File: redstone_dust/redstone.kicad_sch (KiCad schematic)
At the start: 42 parts, among them J1 Conn_01x04_MountingPin, J2 Conn_01x04_MountingPin, J3 Conn_01x04_MountingPin, J4 Conn_01x04_MountingPin, J5 Conn_01x04_MountingPin, J6 Conn_01x04_MountingPin, J7 Conn_01x04_MountingPin, J8 Conn_01x04_MountingPin, Q1 BC108, Q2 BC108, Q3 BC108, Q4 BC108, SW1 SW_Push_Open, U1 RP2040, U2 RBT05W24S05, U3 TPS62162DSG, U4 W25Q16JVSS, U5 W25Q16JVSS

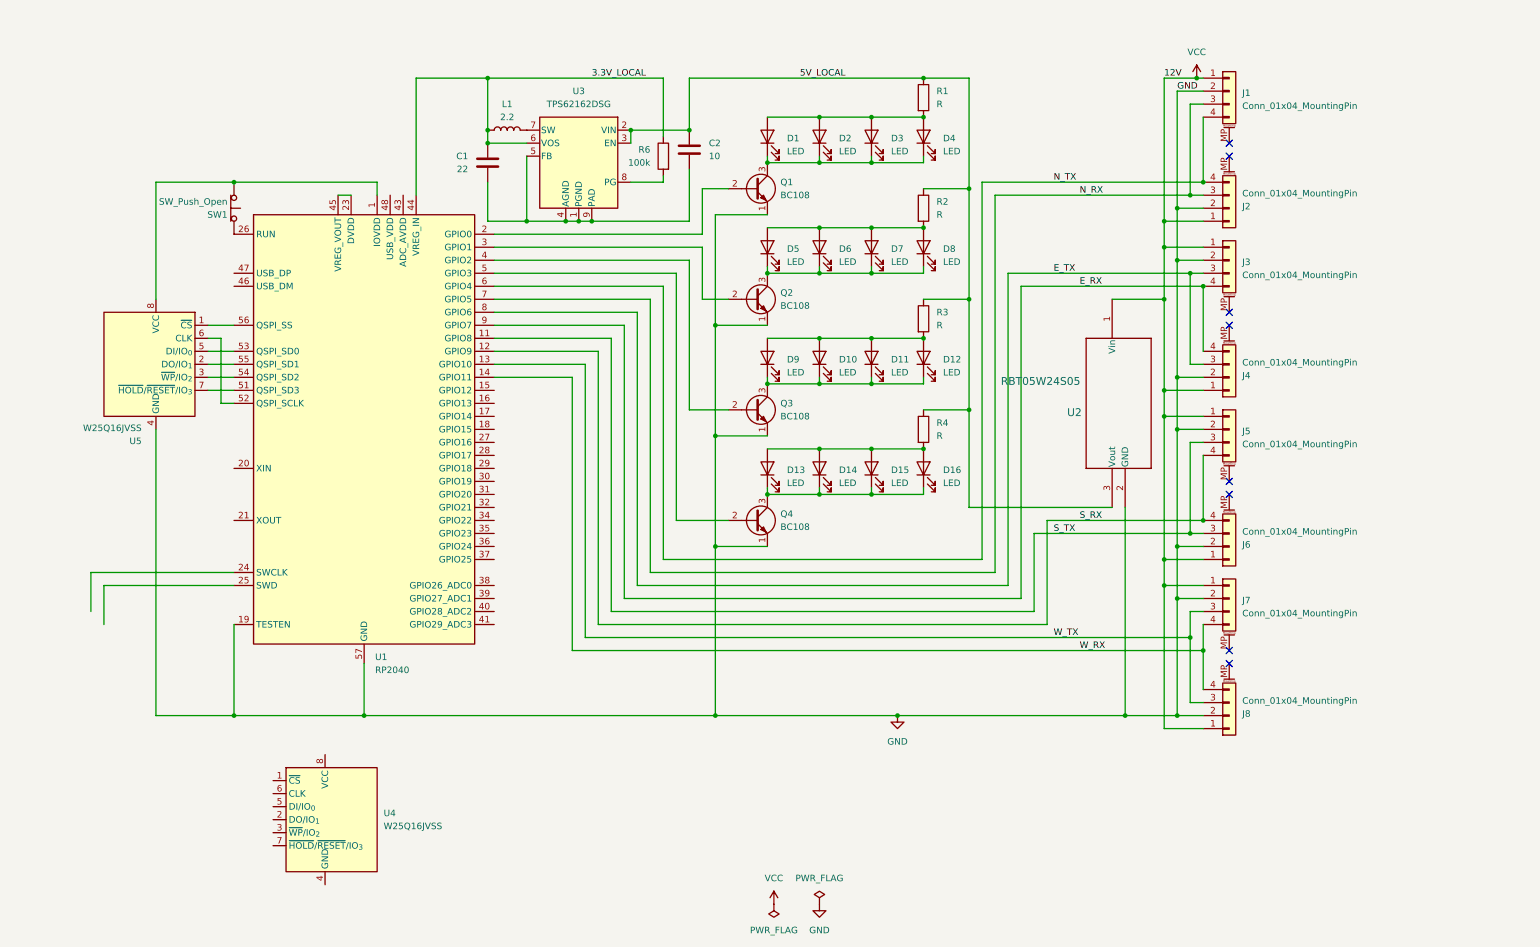
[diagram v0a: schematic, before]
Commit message: add resistors with proper values
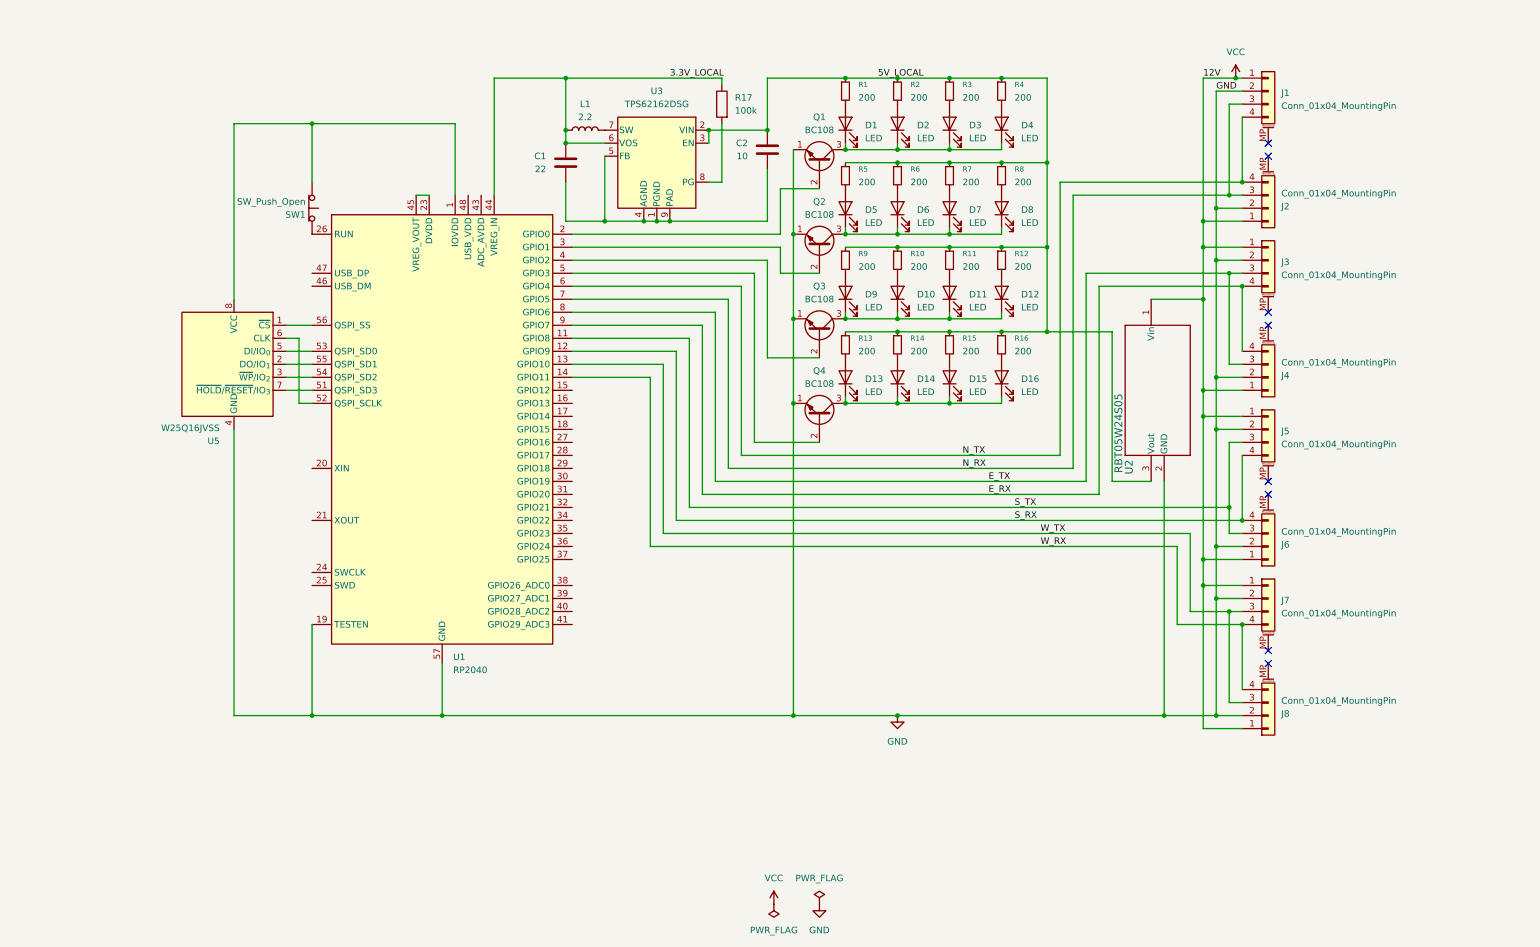
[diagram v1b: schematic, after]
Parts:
- removed R1, R2, R3, R4: R, symbol Device:R
- removed R6: 100k, symbol Device:R
- removed U4: W25Q16JVSS, Package_SO:SOIC-8_5.3x5.3mm_P1.27mm, symbol Memory_Flash:W25Q16JVSS
- added R1, R10, R11, R12, R13, R14, R15, R16, R2, R3, R4, R5, R6, R7, R8, R9: 200, symbol Device:R_Small
- added R17: 100k, symbol Device:R
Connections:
- net 3.3V_LOCAL: now also R17.1
- net 5V_LOCAL: now also R1.1, R10.1, R11.1, R12.1, R13.1, R14.1, R15.1, R16.1, R2.1, R3.1, R4.1, R5.1, R6.1, R7.1, R8.1, R9.1
- net at U3.8 (PG): now also R17.2
- new net: D7.2 (A), R7.2
- new net: D3.2 (A), R3.2
- new net: D12.2 (A), R12.2
- new net: D2.2 (A), R2.2
- new net: D4.2 (A), R4.2
- new net: D10.2 (A), R10.2
- new net: D14.2 (A), R14.2
- new net: D6.2 (A), R6.2
- new net: D5.2 (A), R5.2
- new net: D15.2 (A), R15.2
- new net: D8.2 (A), R8.2
- new net: D1.2 (A), R1.2
- new net: D13.2 (A), R13.2
- new net: D9.2 (A), R9.2
- new net: D11.2 (A), R11.2
- new net: D16.2 (A), R16.2
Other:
- moved on the sheet: C1, C2, D1, D10, D11, D12, D13, D14, D15, D16, D2, D3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

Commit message: add tvs diode and reorganize wiring
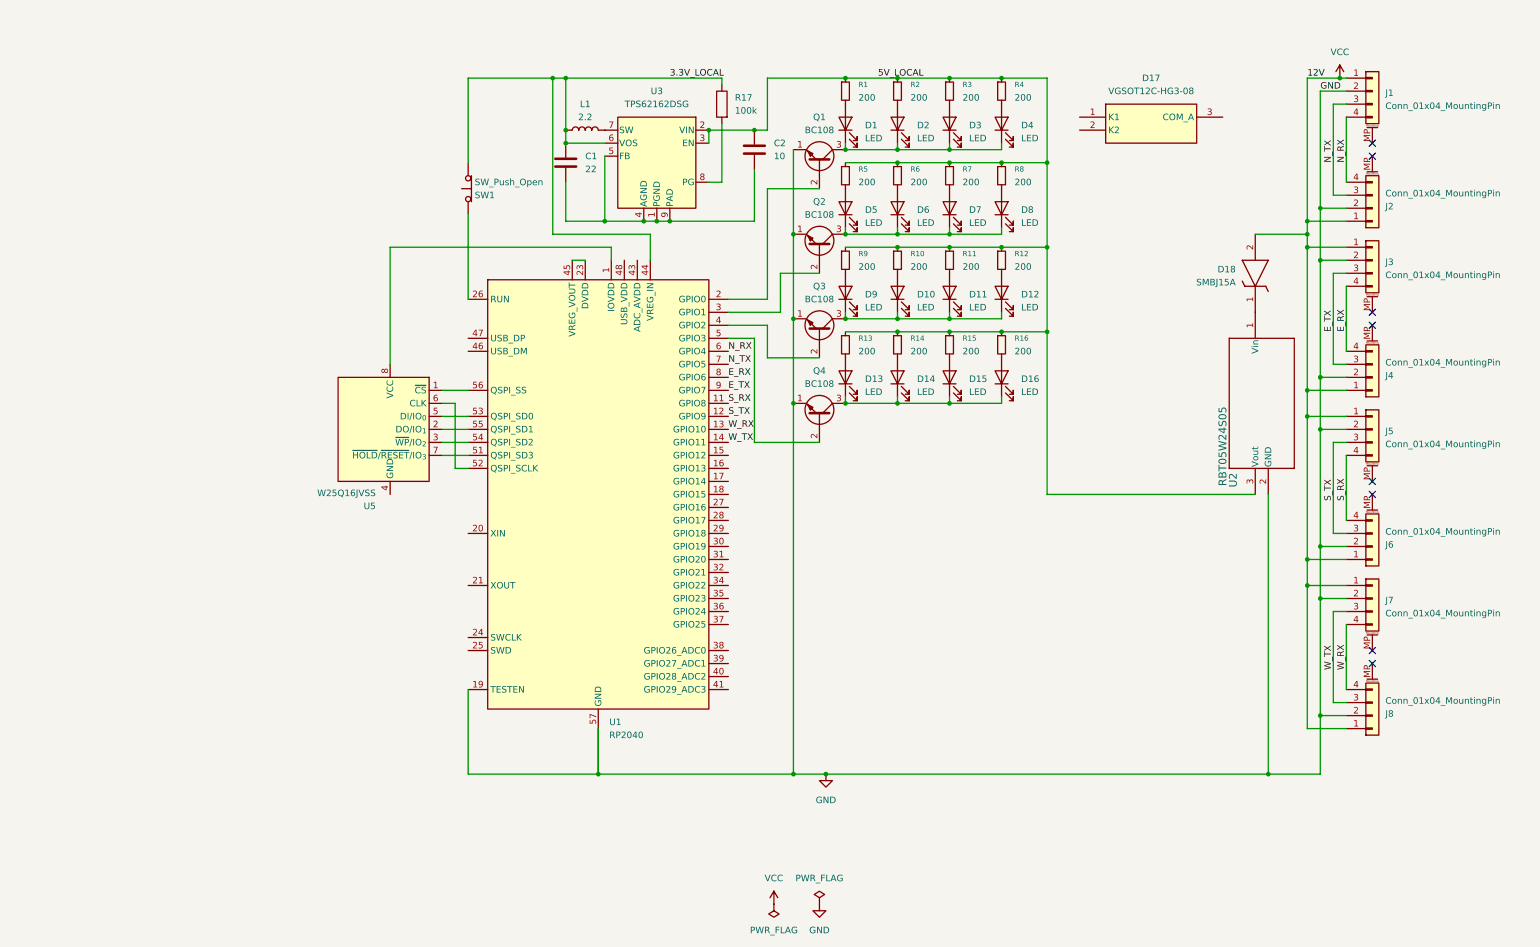
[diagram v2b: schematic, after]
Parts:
- added D17: VGSOT12C-HG3-08, SOT95P242X112-3N, symbol SamacSys_Parts:VGSOT12C-HG3-08
- added D18: SMBJ15A, DIOM5436X244N, symbol SamacSys_Parts:SMBJ15A
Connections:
- net 3.3V_LOCAL: now also SW1.1 (A)
- net E_RX: now also U1.8 (GPIO6); no longer U1.9 (GPIO7)
- net E_TX: now also U1.9 (GPIO7); no longer U1.8 (GPIO6)
- net GND: no longer U5.4 (GND)
- net N_RX: now also J1.4 (Pin_4), J2.4 (Pin_4), U1.6 (GPIO4); no longer J1.3 (Pin_3), J2.3 (Pin_3), U1.7 (GPIO5)
- net N_TX: now also J1.3 (Pin_3), J2.3 (Pin_3), U1.7 (GPIO5); no longer J1.4 (Pin_4), J2.4 (Pin_4), U1.6 (GPIO4)
- net S_RX: now also U1.11 (GPIO8); no longer U1.12 (GPIO9)
- net S_TX: now also U1.12 (GPIO9); no longer U1.11 (GPIO8)
- net VCC: now also D18.2 (A); no longer U2.1 (Vin)
- net W_RX: now also U1.13 (GPIO10); no longer U1.14 (GPIO11)
- net W_TX: now also U1.14 (GPIO11); no longer U1.13 (GPIO10)
- net at U1.1 (IOVDD), U1.10 (IOVDD), U1.22 (IOVDD)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: no longer SW1.1 (A)
- new net: D18.1 (K), U2.1 (Vin)
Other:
- moved on the sheet: C2, J1, J2, J3, J4, J5, J6, J7, J8, SW1, U1, U2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

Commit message: add tps diodes for rx tx
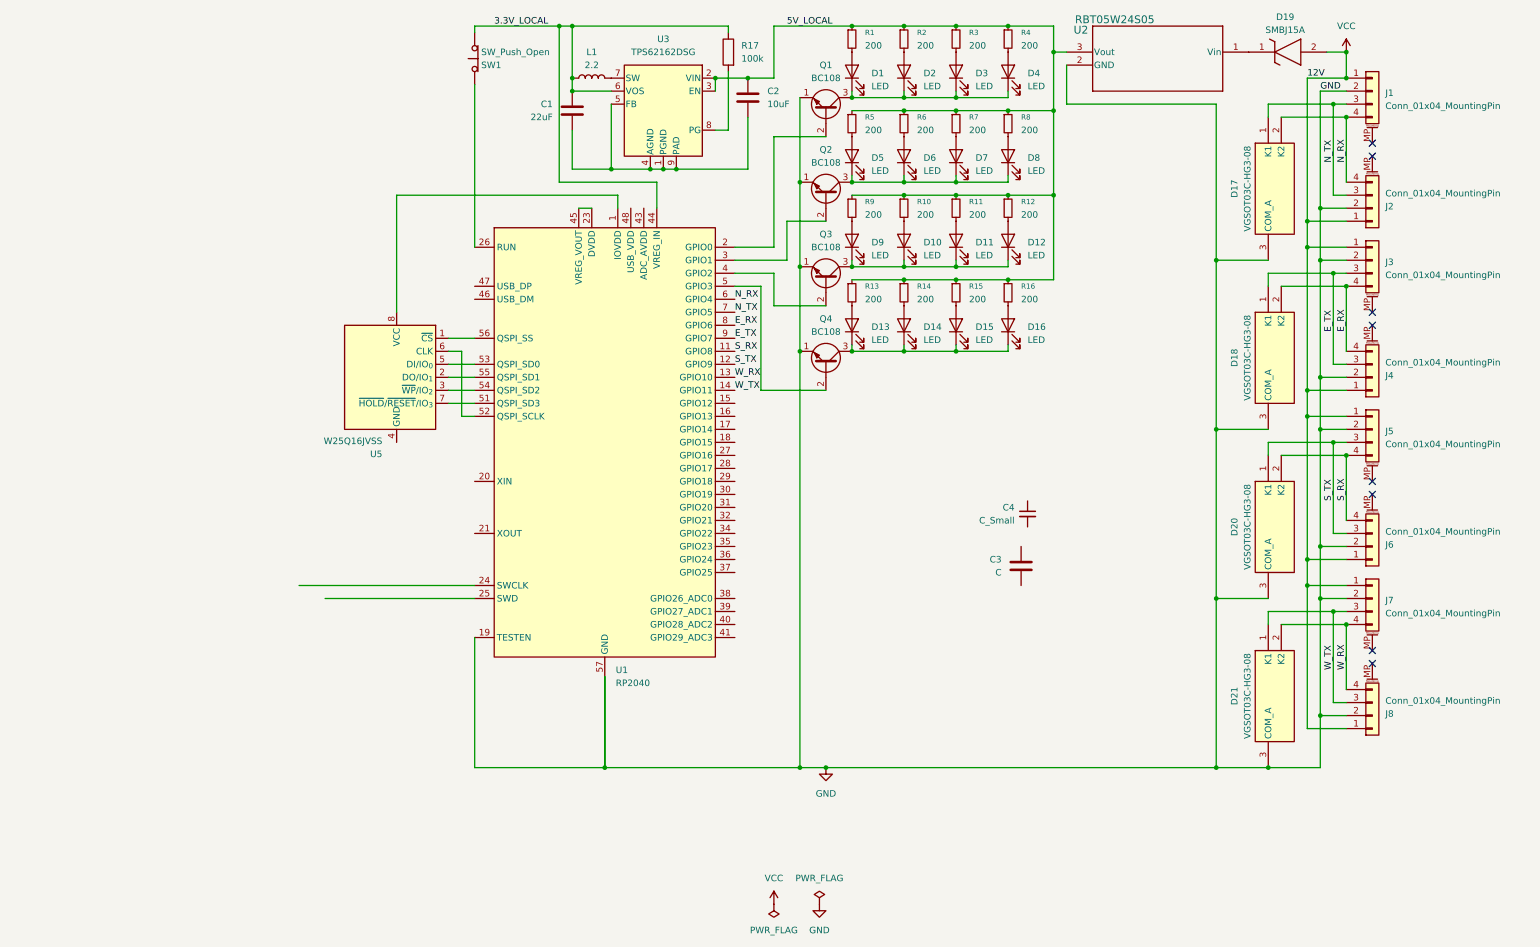
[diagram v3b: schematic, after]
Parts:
- removed D17: VGSOT12C-HG3-08, SOT95P242X112-3N, symbol SamacSys_Parts:VGSOT12C-HG3-08
- removed D18: SMBJ15A, DIOM5436X244N, symbol SamacSys_Parts:SMBJ15A
- added C3: C, symbol Device:C
- added C4: C_Small, symbol Device:C_Small
- added D17, D18, D20, D21: VGSOT03C-HG3-08, SOT95P248X115-3N, symbol SamacSys_Parts:VGSOT03C-HG3-08
- added D19: SMBJ15A, DIOM5436X244N, symbol SamacSys_Parts:SMBJ15A
- C1: value 22 -> 22uF
- C2: value 10 -> 10uF
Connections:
- net E_RX: now also D18.2 (K2)
- net E_TX: now also D18.1 (K1)
- net GND: now also D17.3 (COM_A), D18.3 (COM_A), D20.3 (COM_A), D21.3 (COM_A)
- net N_RX: now also D17.2 (K2)
- net N_TX: now also D17.1 (K1)
- net S_RX: now also D20.2 (K2)
- net S_TX: now also D20.1 (K1)
- net VCC: now also D19.2 (A)
- net W_RX: now also D21.2 (K2)
- net W_TX: now also D21.1 (K1)
- net at U2.1 (Vin): now also D19.1 (K)
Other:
- moved on the sheet: C1, C2, D1, D10, D11, D12, D13, D14, D15, D16, D2, D3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

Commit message: add decoupling capacitors
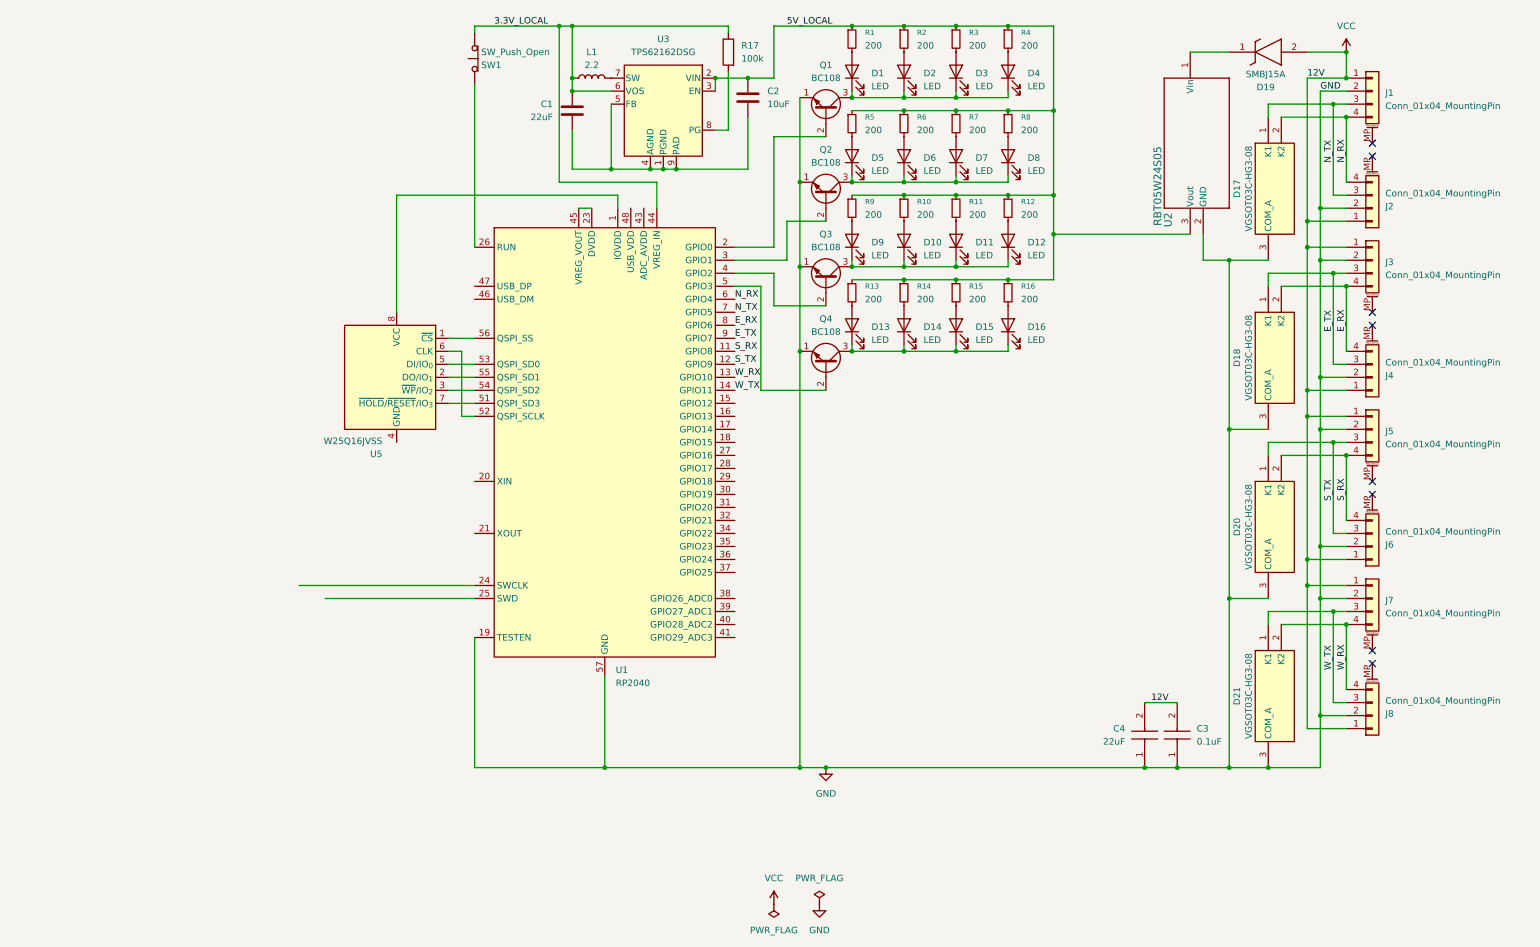
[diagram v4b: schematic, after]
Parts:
- removed C3: C, symbol Device:C
- removed C4: C_Small, symbol Device:C_Small
- added C3: 0.1uF, CAPC2012X140N, symbol SamacSys_Parts:C0805F104K1RACAUTO
- added C4: 22uF, GRM18x, symbol SamacSys_Parts:GRM188C81A226ME01D
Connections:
- net GND: now also C3.1, C4.1
- net VCC: now also C3.2, C4.2
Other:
- moved on the sheet: D19, U2

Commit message: add programming pins
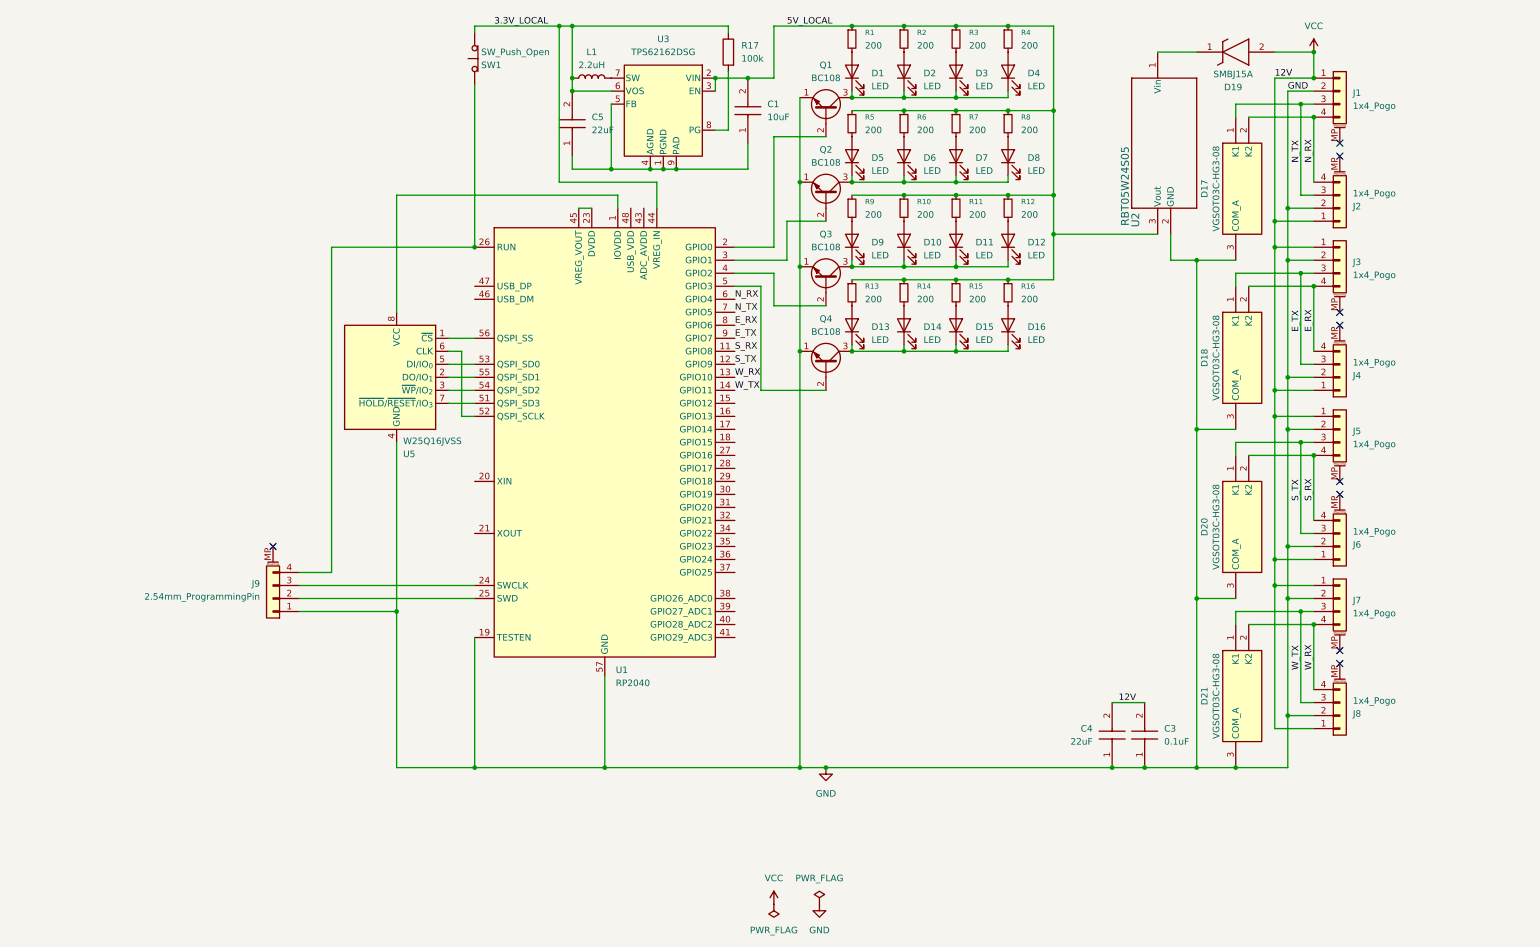
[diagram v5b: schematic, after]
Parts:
- removed C1: 22uF, symbol Device:C
- removed C2: 10uF, symbol Device:C
- added C1: 10uF, CAPC1005X70N, symbol SamacSys_Parts:GRM155R60J106ME18D
- added C5: 22uF, GRM18x, symbol SamacSys_Parts:GRM188C81A226ME01D
- added J9: 2.54mm_ProgrammingPin, symbol Connector_Generic_MountingPin:Conn_01x04_MountingPin
- J1, J2, J3, J4, J5, J6, J7, J8: value Conn_01x04_MountingPin -> 1x4_Pogo
- L1: value 2.2 -> 2.2uH; footprint (none) -> SamacSys_Parts:LCENA2016MKT2R2M0NK
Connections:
- net 3.3V_LOCAL: now also C5.2
- net 5V_LOCAL: now also C1.2
- net GND: now also U5.4 (GND), J9.1 (Pin_1)
- net at U3.1 (PGND), U3.4 (AGND), U3.5 (FB)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: now also C1.1, C5.1
- net at U1.24 (SWCLK): now also J9.3 (Pin_3)
- net at U1.25 (SWD): now also J9.2 (Pin_2)
- net at SW1.2 (B), U1.26 (RUN): now also J9.4 (Pin_4)
- no-connect marks 8 -> 9
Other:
- moved on the sheet: C3, C4, D17, D18, D19, D20, D21, J1, J2, J3, J4, J5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
